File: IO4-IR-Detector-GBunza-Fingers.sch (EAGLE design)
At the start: 3 parts

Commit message: 1.0-panel
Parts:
- added J10, J11, J12, J13, J14, J15, J16, J2, J3, J4, J5, J6, J7, J8, J9: (no value), SPCoast:CONNECTOR-M04LOCK
- added T.AMBIENT1, T.AMBIENT10, T.AMBIENT11, T.AMBIENT12, T.AMBIENT13, T.AMBIENT14, T.AMBIENT15, T.AMBIENT2, T.AMBIENT3, T.AMBIENT4, T.AMBIENT5, T.AMBIENT6, T.AMBIENT7, T.AMBIENT8, T.AMBIENT9, T.DETECTED1, T.DETECTED10, T.DETECTED11, T.DETECTED12, T.DETECTED13, T.DETECTED14, T.DETECTED15, T.DETECTED2, T.DETECTED3, T.DETECTED4, T.DETECTED5, T.DETECTED6, T.DETECTED7, T.DETECTED8, T.DETECTED9: PT19-21C/L41, SparkFun-Sensors:LIGHTSENSORALS
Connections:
- new net N$1: J2.4, T.AMBIENT1.E1
- new net N$10: J4.1, T.DETECTED3.E1
- new net N$11: J4.2, T.DETECTED3.C1
- new net N$12: J4.3, T.AMBIENT3.C1
- new net N$17: J5.4, T.AMBIENT4.E1
- new net N$18: J5.1, T.DETECTED4.E1
- new net N$19: J5.2, T.DETECTED4.C1
- new net N$2: J2.1, T.DETECTED1.E1
- new net N$20: J5.3, T.AMBIENT4.C1
- new net N$21: J6.4, T.AMBIENT5.E1
- new net N$22: J6.1, T.DETECTED5.E1
- new net N$23: J6.2, T.DETECTED5.C1
- new net N$24: J6.3, T.AMBIENT5.C1
- new net N$25: J7.4, T.AMBIENT6.E1
- new net N$26: J7.1, T.DETECTED6.E1
- new net N$27: J7.2, T.DETECTED6.C1
- new net N$28: J7.3, T.AMBIENT6.C1
- new net N$29: J8.4, T.AMBIENT7.E1
- new net N$3: J2.2, T.DETECTED1.C1
- new net N$30: J8.1, T.DETECTED7.E1
- new net N$31: J8.2, T.DETECTED7.C1
- new net N$32: J8.3, T.AMBIENT7.C1
- new net N$33: J9.4, T.AMBIENT8.E1
- new net N$34: J9.1, T.DETECTED8.E1
- new net N$35: J9.2, T.DETECTED8.C1
- new net N$36: J9.3, T.AMBIENT8.C1
- new net N$37: J10.4, T.AMBIENT9.E1
- new net N$38: J10.1, T.DETECTED9.E1
- new net N$39: J10.2, T.DETECTED9.C1
- new net N$4: J2.3, T.AMBIENT1.C1
- new net N$40: J10.3, T.AMBIENT9.C1
- new net N$41: J11.4, T.AMBIENT10.E1
- new net N$42: J11.1, T.DETECTED10.E1
- new net N$43: J11.2, T.DETECTED10.C1
- new net N$44: J11.3, T.AMBIENT10.C1
- new net N$45: J12.4, T.AMBIENT11.E1
- new net N$46: J12.1, T.DETECTED11.E1
- new net N$47: J12.2, T.DETECTED11.C1
- new net N$48: J12.3, T.AMBIENT11.C1
- new net N$49: J13.4, T.AMBIENT12.E1
- new net N$5: J3.4, T.AMBIENT2.E1
- new net N$50: J13.1, T.DETECTED12.E1
- new net N$51: J13.2, T.DETECTED12.C1
- new net N$52: J13.3, T.AMBIENT12.C1
- new net N$53: J14.4, T.AMBIENT13.E1
- new net N$54: J14.1, T.DETECTED13.E1
- new net N$55: J14.2, T.DETECTED13.C1
- new net N$56: J14.3, T.AMBIENT13.C1
- new net N$57: J15.4, T.AMBIENT14.E1
- new net N$58: J15.1, T.DETECTED14.E1
- new net N$59: J15.2, T.DETECTED14.C1
- new net N$6: J3.1, T.DETECTED2.E1
- new net N$60: J15.3, T.AMBIENT14.C1
- new net N$61: J16.4, T.AMBIENT15.E1
- new net N$62: J16.1, T.DETECTED15.E1
- new net N$63: J16.2, T.DETECTED15.C1
- new net N$64: J16.3, T.AMBIENT15.C1
- new net N$7: J3.2, T.DETECTED2.C1
- new net N$8: J3.3, T.AMBIENT2.C1
- new net N$9: J4.4, T.AMBIENT3.E1

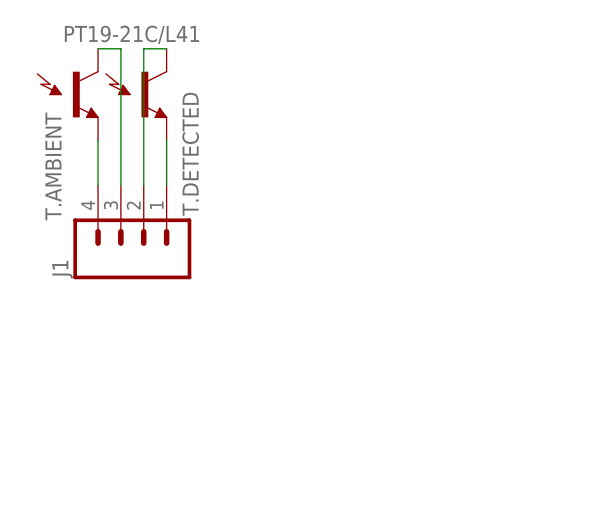
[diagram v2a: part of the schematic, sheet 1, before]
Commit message: added values for connectors
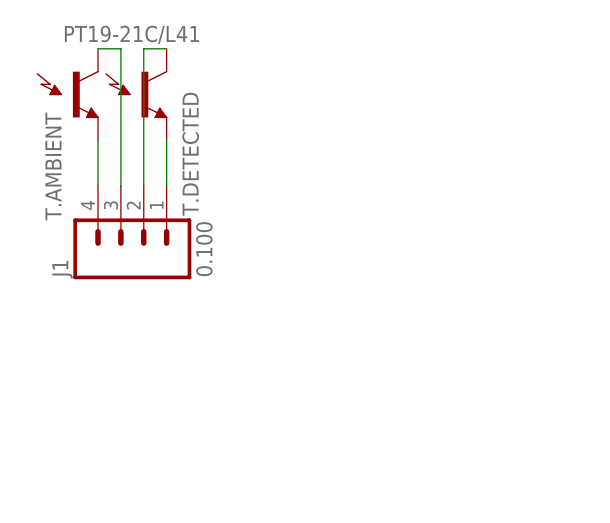
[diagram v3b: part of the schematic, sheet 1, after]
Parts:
- J1, J10, J11, J12, J13, J14, J15, J16, J2, J3, J4, J5, J6, J7, J8, J9: value (none) -> 0.100
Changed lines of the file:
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@@
 <setting verticaltext="up"/>
 </settings>
-<grid distance="0.1" unitdist="inch" unit="inch" style="lines" multiple="1" display="no" altdistance="0.01" altunitdist="inch" altunit="inch"/>
+<grid distance="100" unitdist="mil" unit="mil" style="dots" multiple="1" display="yes" altdistance="50" altunitdist="mil" altunit="mil"/>
 <layers>
 <layer number="1" name="Top" color="4" fill="1" visible="no" active="no"/>
@@
 <part name="T.AMBIENT" library="SparkFun-Sensors" deviceset="LIGHTSENSOR" device="ALS" value="PT19-21C/L41"/>
 <part name="T.DETECTED" library="SparkFun-Sensors" deviceset="LIGHTSENSOR" device="ALS" value="PT19-21C/L41"/>
-<part name="J1" library="SPCoast" deviceset="CONNECTOR-M04" device="LOCK"/>
+<part name="J1" library="SPCoast" deviceset="CONNECTOR-M04" device="LOCK" value="0.100"/>
 <part name="FRAME3" library="SPCoast" deviceset="DOC-FRAME-LETTER" device=""/>
 <part name="T.AMBIENT1" library="SparkFun-Sensors" deviceset="LIGHTSENSOR" device="ALS" value="PT19-21C/L41"/>
 <part name="T.DETECTED1" library="SparkFun-Sensors" deviceset="LIGHTSENSOR" device="ALS" value="PT19-21C/L41"/>
-<part name="J2" library="SPCoast" deviceset="CONNECTOR-M04" device="LOCK"/>
+<part name="J2" library="SPCoast" deviceset="CONNECTOR-M04" device="LOCK" value="0.100"/>
 <part name="FRAME4" library="SPCoast" deviceset="DOC-FRAME-LETTER" device=""/>
 <part name="T.AMBIENT2" library="SparkFun-Sensors" deviceset="LIGHTSENSOR" device="ALS" value="PT19-21C/L41"/>
 <part name="T.DETECTED2" library="SparkFun-Sensors" deviceset="LIGHTSENSOR" device="ALS" value="PT19-21C/L41"/>
-<part name="J3" library="SPCoast" deviceset="CONNECTOR-M04" device="LOCK"/>
+<part name="J3" library="SPCoast" deviceset="CONNECTOR-M04" device="LOCK" value="0.100"/>
 <part name="FRAME5" library="SPCoast" deviceset="DOC-FRAME-LETTER" device=""/>
 <part name="T.AMBIENT3" library="SparkFun-Sensors" deviceset="LIGHTSENSOR" device="ALS" value="PT19-21C/L41"/>
 <part name="T.DETECTED3" library="SparkFun-Sensors" deviceset="LIGHTSENSOR" device="ALS" value="PT19-21C/L41"/>
-<part name="J4" library="SPCoast" deviceset="CONNECTOR-M04" device="LOCK"/>
+<part name="J4" library="SPCoast" deviceset="CONNECTOR-M04" device="LOCK" value="0.100"/>
 <part name="FRAME6" library="SPCoast" deviceset="DOC-FRAME-LETTER" device=""/>
 <part name="T.AMBIENT4" library="SparkFun-Sensors" deviceset="LIGHTSENSOR" device="ALS" value="PT19-21C/L41"/>
 <part name="T.DETECTED4" library="SparkFun-Sensors" deviceset="LIGHTSENSOR" device="ALS" value="PT19-21C/L41"/>
-<part name="J5" library="SPCoast" deviceset="CONNECTOR-M04" device="LOCK"/>
+<part name="J5" library="SPCoast" deviceset="CONNECTOR-M04" device="LOCK" value="0.100"/>
 <part name="FRAME7" library="SPCoast" deviceset="DOC-FRAME-LETTER" device=""/>
 <part name="T.AMBIENT5" library="SparkFun-Sensors" deviceset="LIGHTSENSOR" device="ALS" value="PT19-21C/L41"/>
 <part name="T.DETECTED5" library="SparkFun-Sensors" deviceset="LIGHTSENSOR" device="ALS" value="PT19-21C/L41"/>
-<part name="J6" library="SPCoast" deviceset="CONNECTOR-M04" device="LOCK"/>
+<part name="J6" library="SPCoast" deviceset="CONNECTOR-M04" device="LOCK" value="0.100"/>
 <part name="FRAME8" library="SPCoast" deviceset="DOC-FRAME-LETTER" device=""/>
 <part name="T.AMBIENT6" library="SparkFun-Sensors" deviceset="LIGHTSENSOR" device="ALS" value="PT19-21C/L41"/>
 <part name="T.DETECTED6" library="SparkFun-Sensors" deviceset="LIGHTSENSOR" device="ALS" value="PT19-21C/L41"/>
-<part name="J7" library="SPCoast" deviceset="CONNECTOR-M04" device="LOCK"/>
+<part name="J7" library="SPCoast" deviceset="CONNECTOR-M04" device="LOCK" value="0.100"/>
 <part name="FRAME9" library="SPCoast" deviceset="DOC-FRAME-LETTER" device=""/>
 <part name="T.AMBIENT7" library="SparkFun-Sensors" deviceset="LIGHTSENSOR" device="ALS" value="PT19-21C/L41"/>
 <part name="T.DETECTED7" library="SparkFun-Sensors" deviceset="LIGHTSENSOR" device="ALS" value="PT19-21C/L41"/>
-<part name="J8" library="SPCoast" deviceset="CONNECTOR-M04" device="LOCK"/>
+<part name="J8" library="SPCoast" deviceset="CONNECTOR-M04" device="LOCK" value="0.100"/>
 <part name="FRAME10" library="SPCoast" deviceset="DOC-FRAME-LETTER" device=""/>
 <part name="T.AMBIENT8" library="SparkFun-Sensors" deviceset="LIGHTSENSOR" device="ALS" value="PT19-21C/L41"/>
 <part name="T.DETECTED8" library="SparkFun-Sensors" deviceset="LIGHTSENSOR" device="ALS" value="PT19-21C/L41"/>
-<part name="J9" library="SPCoast" deviceset="CONNECTOR-M04" device="LOCK"/>
+<part name="J9" library="SPCoast" deviceset="CONNECTOR-M04" device="LOCK" value="0.100"/>
 <part name="FRAME11" library="SPCoast" deviceset="DOC-FRAME-LETTER" device=""/>
 <part name="T.AMBIENT9" library="SparkFun-Sensors" deviceset="LIGHTSENSOR" device="ALS" value="PT19-21C/L41"/>
 <part name="T.DETECTED9" library="SparkFun-Sensors" deviceset="LIGHTSENSOR" device="ALS" value="PT19-21C/L41"/>
-<part name="J10" library="SPCoast" deviceset="CONNECTOR-M04" device="LOCK"/>
+<part name="J10" library="SPCoast" deviceset="CONNECTOR-M04" device="LOCK" value="0.100"/>
 <part name="FRAME12" library="SPCoast" deviceset="DOC-FRAME-LETTER" device=""/>
 <part name="T.AMBIENT10" library="SparkFun-Sensors" deviceset="LIGHTSENSOR" device="ALS" value="PT19-21C/L41"/>
 <part name="T.DETECTED10" library="SparkFun-Sensors" deviceset="LIGHTSENSOR" device="ALS" value="PT19-21C/L41"/>
-<part name="J11" library="SPCoast" deviceset="CONNECTOR-M04" device="LOCK"/>
+<part name="J11" library="SPCoast" deviceset="CONNECTOR-M04" device="LOCK" value="0.100"/>
 <part name="FRAME13" library="SPCoast" deviceset="DOC-FRAME-LETTER" device=""/>
 <part name="T.AMBIENT11" library="SparkFun-Sensors" deviceset="LIGHTSENSOR" device="ALS" value="PT19-21C/L41"/>
 <part name="T.DETECTED11" library="SparkFun-Sensors" deviceset="LIGHTSENSOR" device="ALS" value="PT19-21C/L41"/>
-<part name="J12" library="SPCoast" deviceset="CONNECTOR-M04" device="LOCK"/>
+<part name="J12" library="SPCoast" deviceset="CONNECTOR-M04" device="LOCK" value="0.100"/>
 <part name="FRAME14" library="SPCoast" deviceset="DOC-FRAME-LETTER" device=""/>
 <part name="T.AMBIENT12" library="SparkFun-Sensors" deviceset="LIGHTSENSOR" device="ALS" value="PT19-21C/L41"/>
 <part name="T.DETECTED12" library="SparkFun-Sensors" deviceset="LIGHTSENSOR" device="ALS" value="PT19-21C/L41"/>
-<part name="J13" library="SPCoast" deviceset="CONNECTOR-M04" device="LOCK"/>
+<part name="J13" library="SPCoast" deviceset="CONNECTOR-M04" device="LOCK" value="0.100"/>
 <part name="FRAME15" library="SPCoast" deviceset="DOC-FRAME-LETTER" device=""/>
 <part name="T.AMBIENT13" library="SparkFun-Sensors" deviceset="LIGHTSENSOR" device="ALS" value="PT19-21C/L41"/>
 <part name="T.DETECTED13" library="SparkFun-Sensors" deviceset="LIGHTSENSOR" device="ALS" value="PT19-21C/L41"/>
-<part name="J14" library="SPCoast" deviceset="CONNECTOR-M04" device="LOCK"/>
+<part name="J14" library="SPCoast" deviceset="CONNECTOR-M04" device="LOCK" value="0.100"/>
 <part name="FRAME16" library="SPCoast" deviceset="DOC-FRAME-LETTER" device=""/>
 <part name="T.AMBIENT14" library="SparkFun-Sensors" deviceset="LIGHTSENSOR" device="ALS" value="PT19-21C/L41"/>
 <part name="T.DETECTED14" library="SparkFun-Sensors" deviceset="LIGHTSENSOR" device="ALS" value="PT19-21C/L41"/>
-<part name="J15" library="SPCoast" deviceset="CONNECTOR-M04" device="LOCK"/>
+<part name="J15" library="SPCoast" deviceset="CONNECTOR-M04" device="LOCK" value="0.100"/>
 <part name="FRAME17" library="SPCoast" deviceset="DOC-FRAME-LETTER" device=""/>
 <part name="T.AMBIENT15" library="SparkFun-Sensors" deviceset="LIGHTSENSOR" device="ALS" value="PT19-21C/L41"/>
 <part name="T.DETECTED15" library="SparkFun-Sensors" deviceset="LIGHTSENSOR" device="ALS" value="PT19-21C/L41"/>
-<part name="J16" library="SPCoast" deviceset="CONNECTOR-M04" device="LOCK"/>
+<part name="J16" library="SPCoast" deviceset="CONNECTOR-M04" device="LOCK" value="0.100"/>
 </parts>
 <sheets>
